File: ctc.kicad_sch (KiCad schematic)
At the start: 1 part, among them U5 CTC-PLCC-44

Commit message: HW: Update schematic info frames
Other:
- company: (none) -> A.K.
- title: (none) -> Z80 CTC
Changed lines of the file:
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@@
 	(generator_version "9.0")
 	(paper "A4")
+	(title_block
+		(title "Z80 CTC")
+		(date "2025-10-14")
+		(rev "A")
+		(company "A.K.")
+	)
 	(bus_entry
 		(at 93.98 90.17)

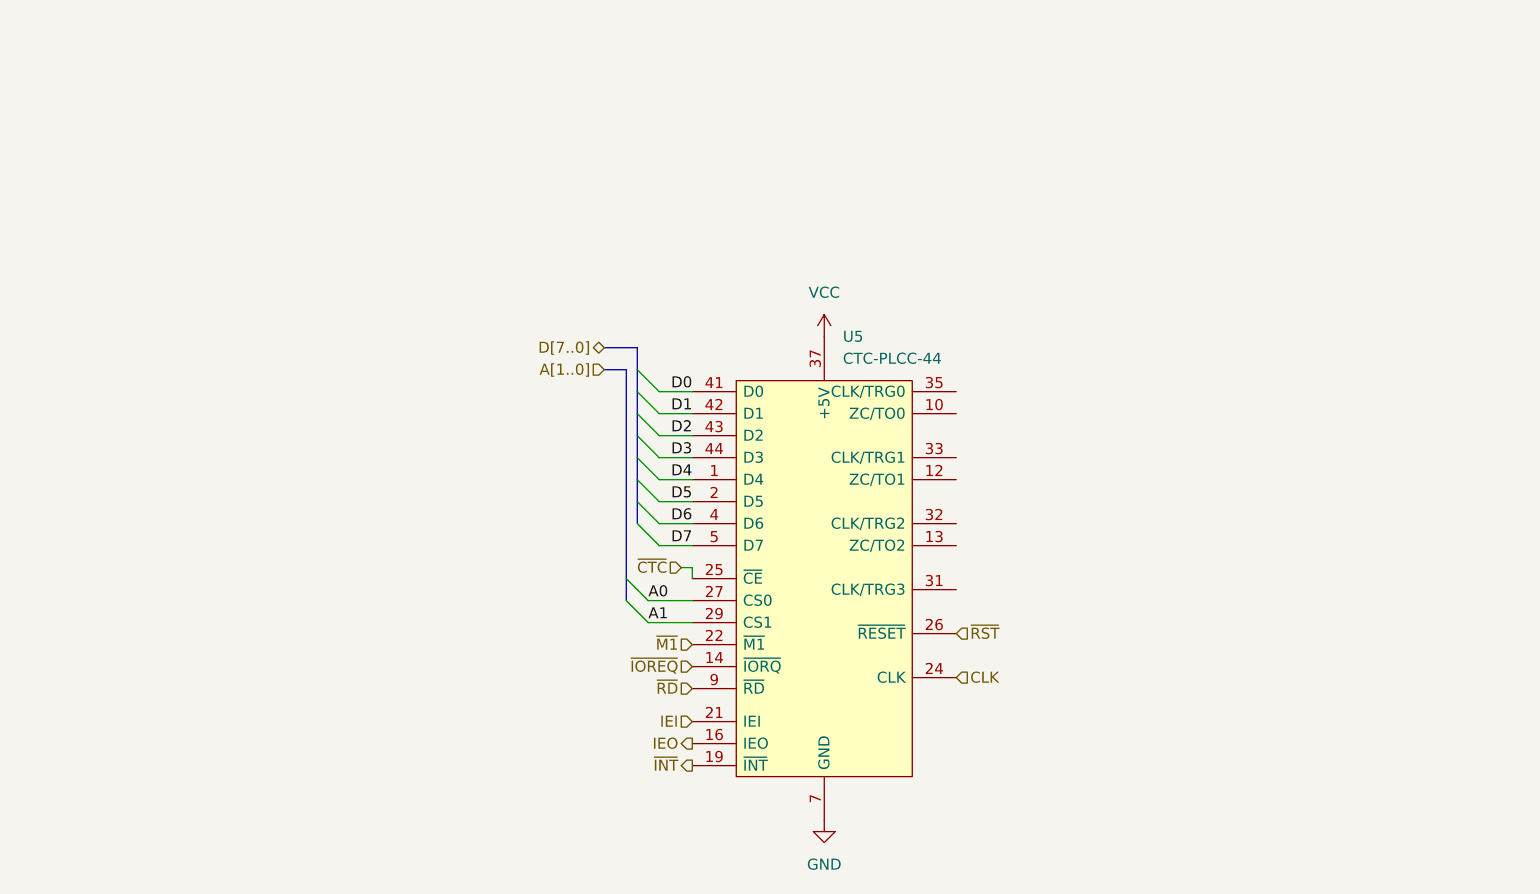
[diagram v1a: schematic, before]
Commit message: HW: Add display, start PCB placement
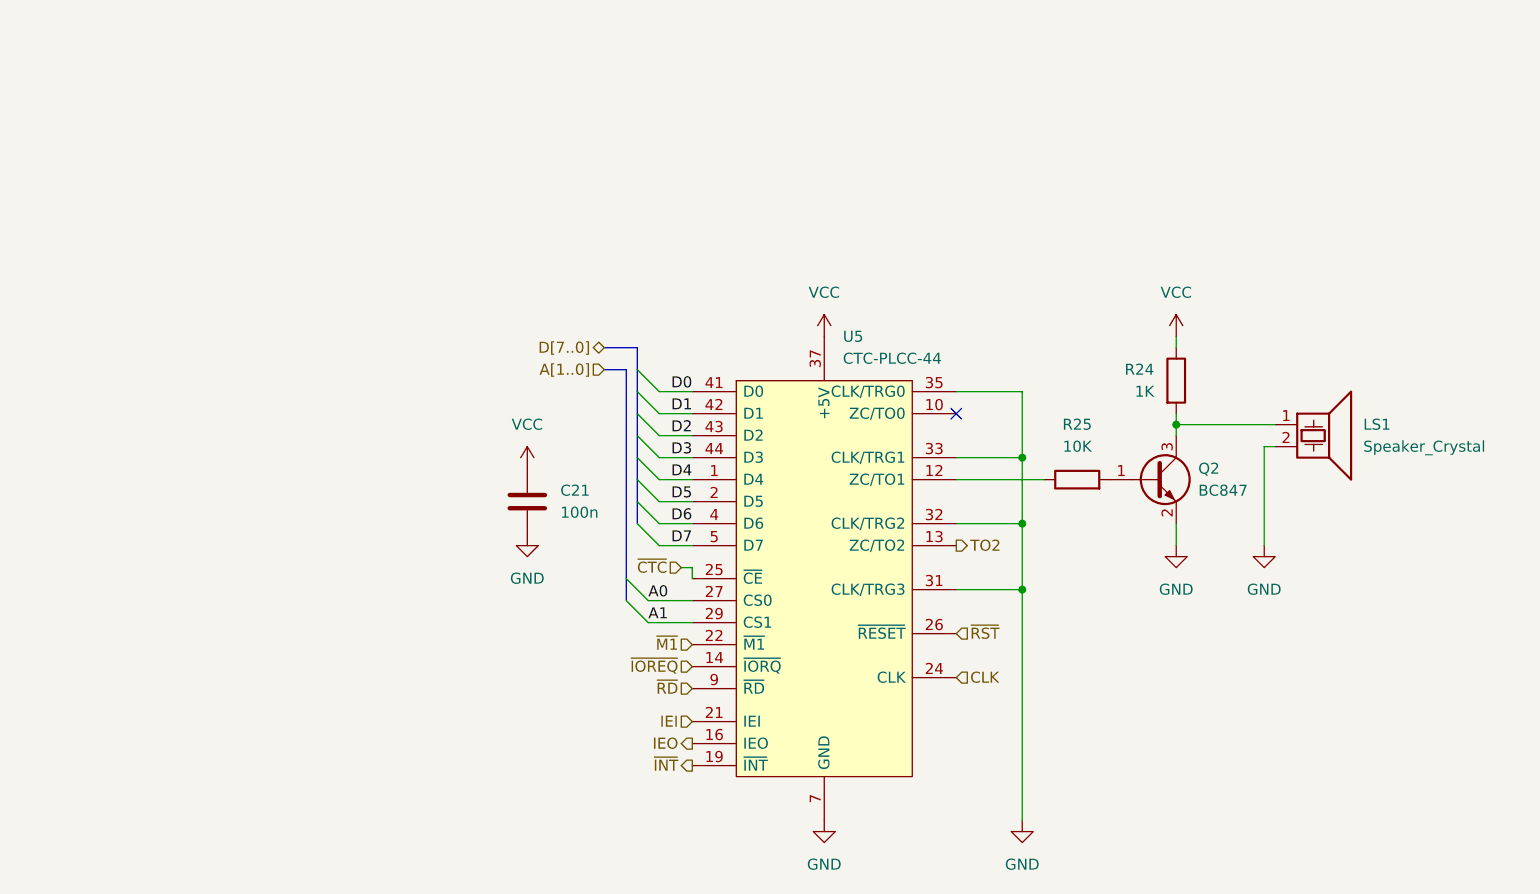
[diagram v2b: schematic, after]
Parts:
- added C21: 100n, Capacitor_SMD:C_0805_2012Metric, symbol Device:C
- added LS1: Speaker_Crystal, Buzzer_Beeper:Buzzer_Murata_PKLCS1212E, symbol Device:Speaker_Crystal
- added Q2: BC847, Package_TO_SOT_SMD:SOT-23, symbol Transistor_BJT:BC847
- added R24: 1K, Resistor_SMD:R_0805_2012Metric, symbol Device:R
- added R25: 10K, Resistor_SMD:R_0805_2012Metric, symbol Device:R
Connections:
- net GND: now also U5.31 (CLK/TRG3), U5.32 (CLK/TRG2), U5.33 (CLK/TRG1), U5.35 (CLK/TRG0), C21.2, LS1.2, Q2.2 (E)
- net VCC: now also C21.1, R24.1
- net at U5.12 (ZC/TO1): now also R25.1
- net TO2: now reaches U5.13 (ZC/TO2)
- new net: LS1.1, Q2.3 (C), R24.2
- new net: Q2.1 (B), R25.2
- no-connect marks 0 -> 1

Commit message: HW: Finish CTC sound generator
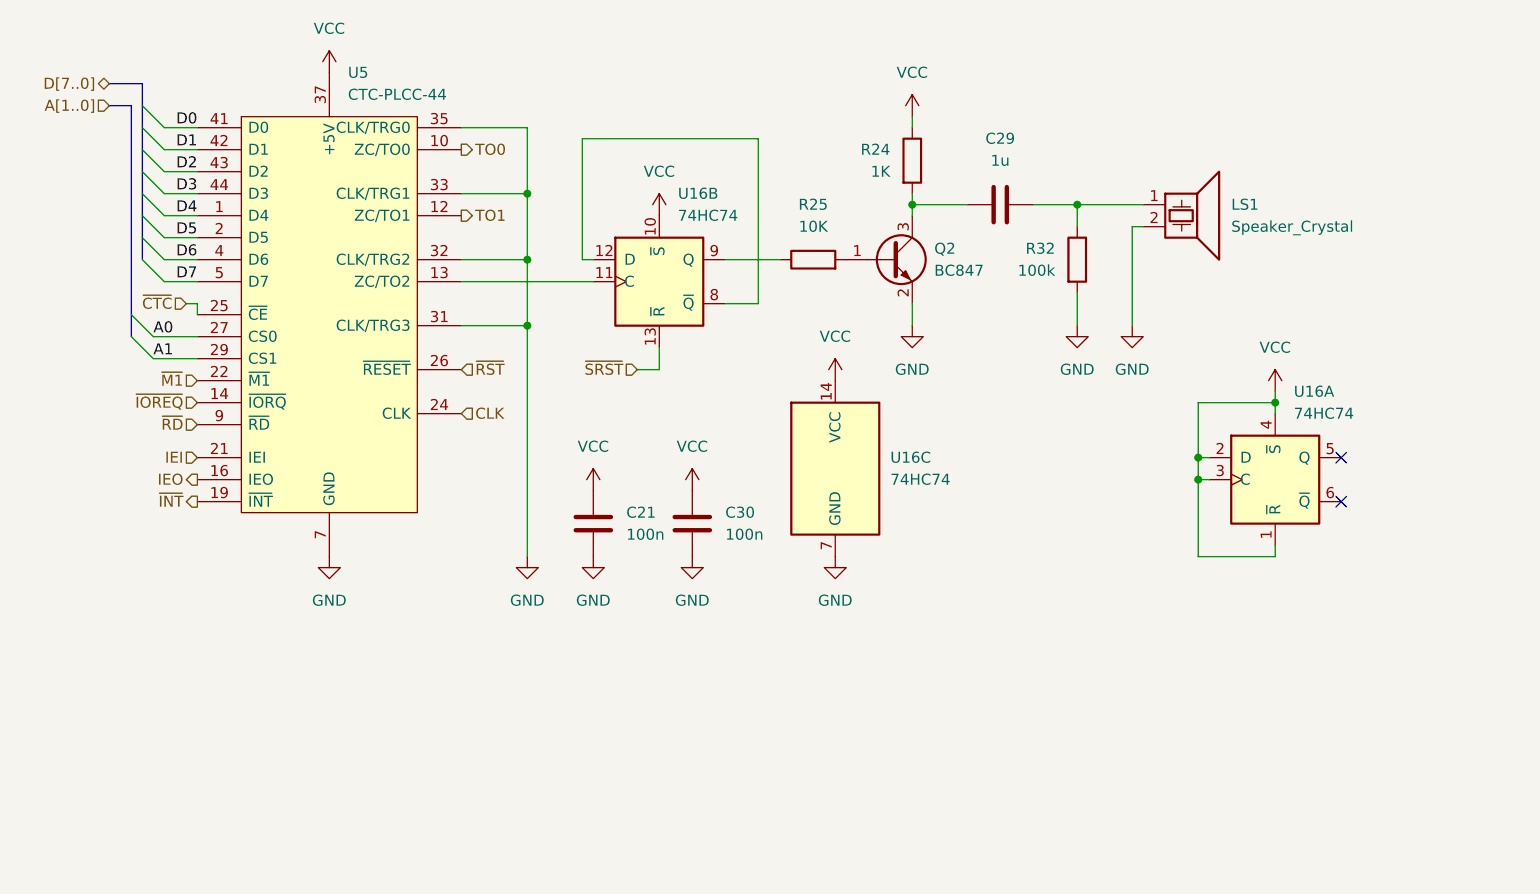
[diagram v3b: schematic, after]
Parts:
- added C29: 1u, Capacitor_SMD:C_0805_2012Metric, symbol Device:C
- added C30: 100n, Capacitor_SMD:C_0805_2012Metric, symbol Device:C
- added R32: 100k, Resistor_SMD:R_0805_2012Metric, symbol Device:R
- added U16: 74HC74, Package_SO:SO-14_3.9x8.65mm_P1.27mm, symbol 74xx:74HC74
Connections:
- net GND: now also C30.2, R32.2, U16.7 (GND)
- net VCC: now also C30.1, U16.1 (~{R}), U16.10 (~{S}), U16.14 (VCC), U16.2 (D), U16.3 (C), U16.4 (~{S})
- net at Q2.3 (C), R24.2: now also C29.1; no longer LS1.1
- net TO0: now reaches U5.10 (ZC/TO0)
- net at R25.1: now also U16.9 (Q); no longer U5.12 (ZC/TO1)
- net TO2: no longer names the net of U5.13 (ZC/TO2)
- net TO2: now also U16.11 (C)
- new net: U16.12 (D), U16.8 (~{Q})
- new net: C29.2, LS1.1, R32.1
- new net TO1: U5.12 (ZC/TO1)
- new net ~{SRST}: U16.13 (~{R})
- no-connect marks 1 -> 2
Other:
- moved on the sheet: C21, LS1, Q2, R24, R25, U5

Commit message: HW: Routing WIP
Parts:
- U5: value CTC-PLCC-44 -> Z80 CTC
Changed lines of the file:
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@@
 			)
 		)
-		(property "Value" "CTC-PLCC-44"
+		(property "Value" "Z80 CTC"
 			(at 61.8333 31.75 0)
 			(effects
